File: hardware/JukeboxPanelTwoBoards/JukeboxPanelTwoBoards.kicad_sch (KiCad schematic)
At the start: 21 parts, among them J1 Raspberry_Pi_2_3, J2 Jukebox Panel, J3 +3.3V, J4 +5V, J5 GND, J6 Display Header, J7 8P8C

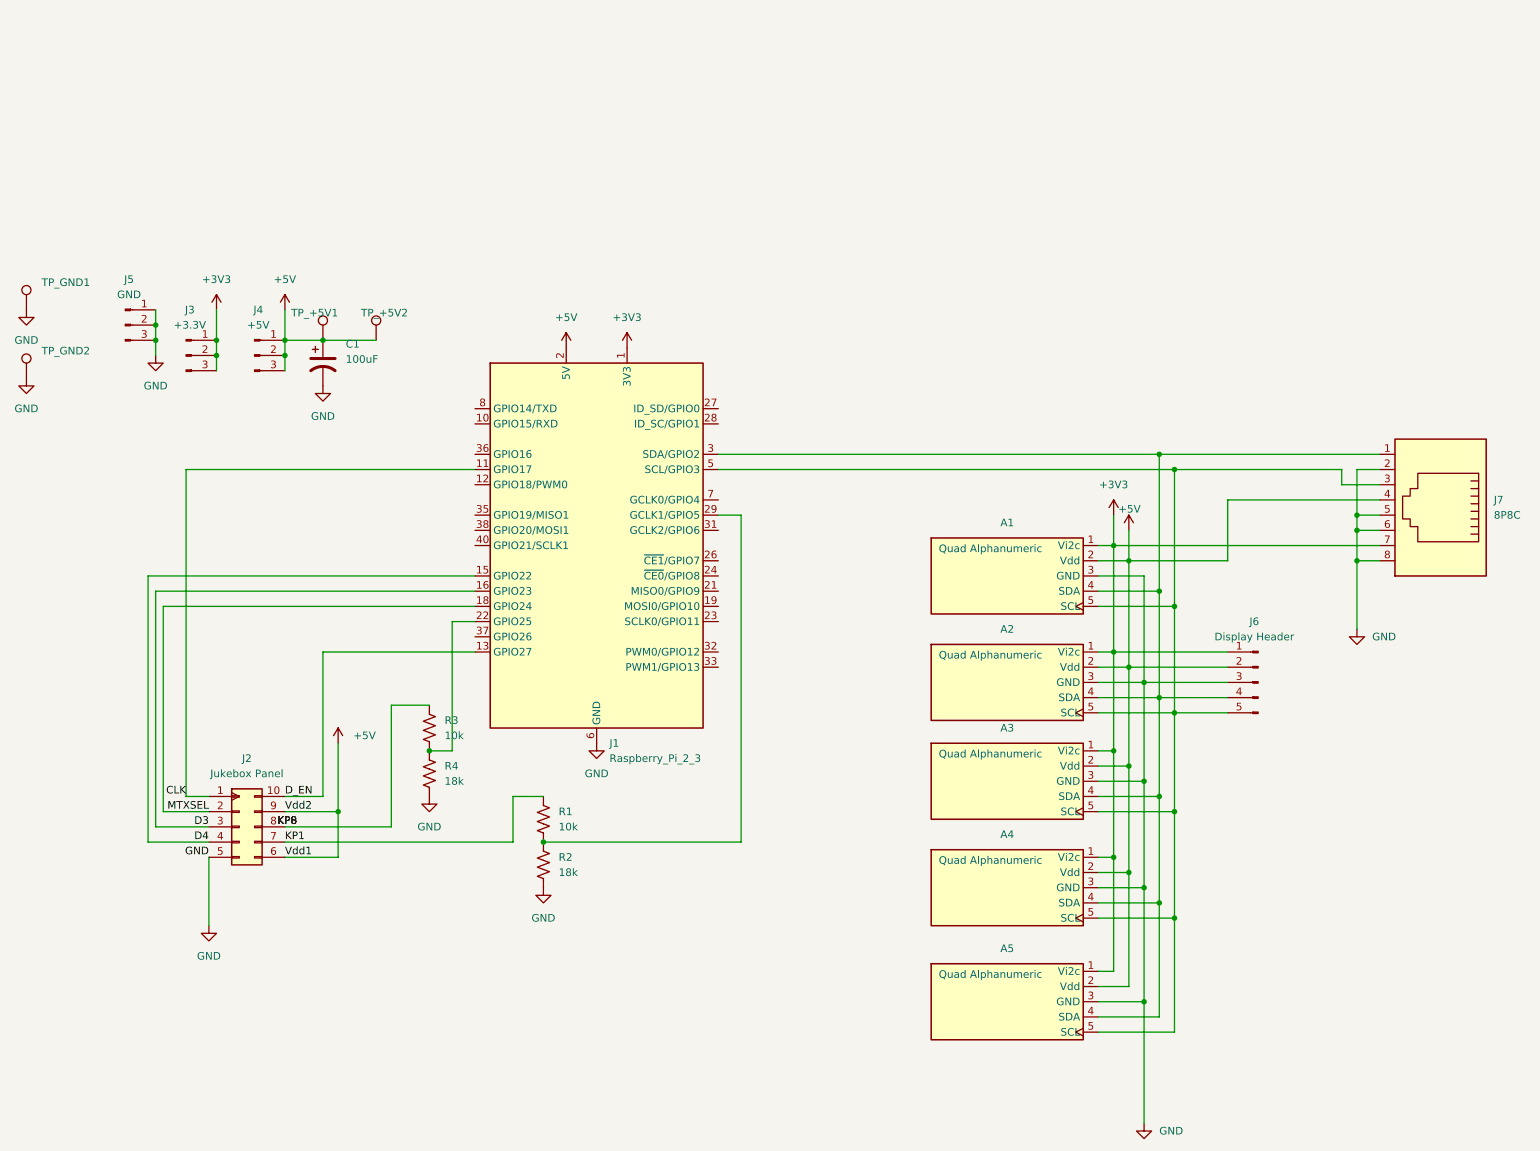
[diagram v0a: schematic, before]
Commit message: Add RJ45 8P8C connector schematic for JukeboxPanelTwoBoards
This commit introduces a new schematic file for the RJ45 8P8C connector used in the JukeboxPanelTwoBoards project. The schematic includes detailed properties, pin configurations, and global labels for power and signal connections. This addition enhances the project's documentation and supports future development and assembly processes.
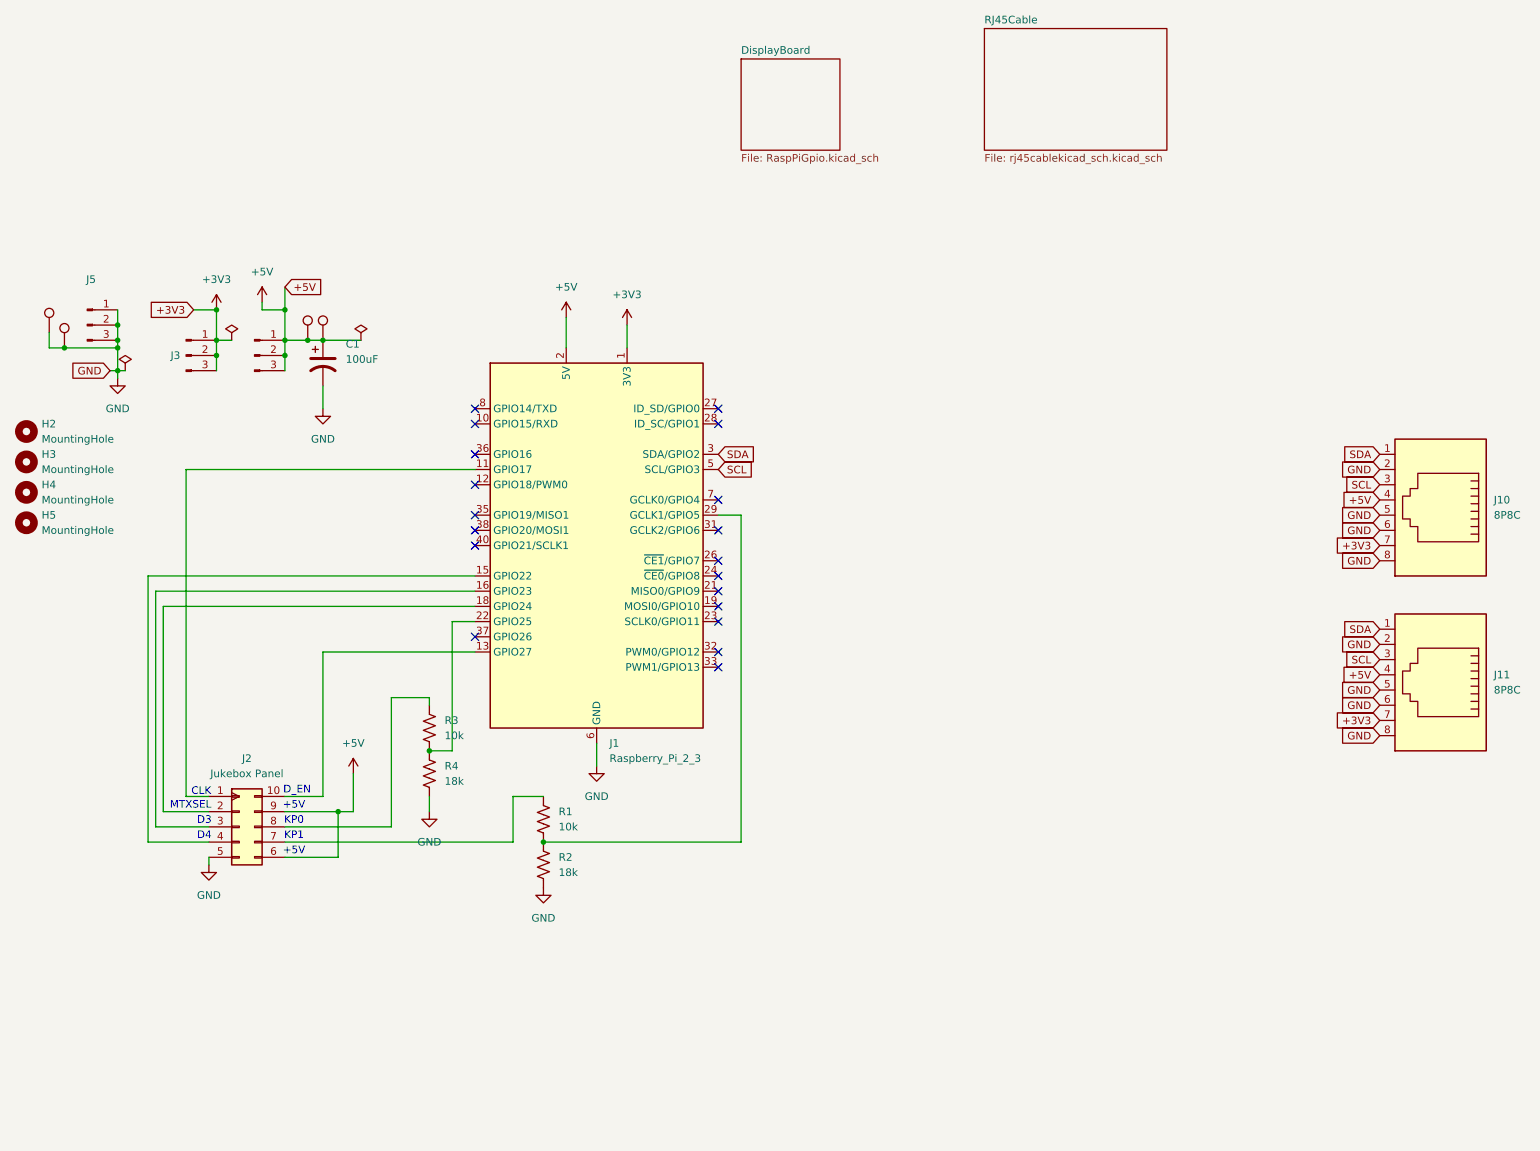
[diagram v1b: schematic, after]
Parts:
- removed A1, A2, A3, A4, A5: Quad Alphanumeric, MyParts:Adafruit_1911_QuadAlphaNum, symbol MyParts:Adafruit_1911_QuadAlphaNum
- removed J6: Display Header, Connector_PinHeader_2.54mm:PinHeader_1x05_P2.54mm_Vertical, symbol Connector:Conn_01x05_Pin
- removed TP_GND1: TestPoint, TestPoint:TestPoint_THTPad_D2.5mm_Drill1.2mm, symbol Connector:TestPoint
- added H2, H3, H4, H5: MountingHole, MountingHole:MountingHole_3.2mm_M3, symbol Mechanical:MountingHole
- added J11: 8P8C, Connector_RJ:RJ45_Ninigi_GE, symbol Connector:8P8C
- added TP_GND3: TestPoint, TestPoint:TestPoint_THTPad_D2.5mm_Drill1.2mm, symbol Connector:TestPoint
- renumbered J7 to J10
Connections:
- net +3V3: now also J11.7
- net +5V: now also J11.4
- net GND: now also J11.2, J11.5, J11.6, J11.8, TP_GND3.1
- net SDA: now reaches J1.3 (SDA/GPIO2), J10.1
- net SDA: now also J11.1
- net SCL: now reaches J1.5 (SCL/GPIO3), J10.3
- net SCL: now also J11.3
- net CLK: no longer names the net of J1.11 (GPIO17), J2.1 (CLK)
- net D3: no longer names the net of J1.16 (GPIO23), J2.3 (D3)
- net D4: no longer names the net of J1.15 (GPIO22), J2.4 (D4)
- net D_EN: no longer names the net of J1.13 (GPIO27), J2.10 (D_EN)
- net KP1: no longer names the net of J2.7 (KP1), R1.1
- net MTXSEL: no longer names the net of J1.18 (GPIO24), J2.2 (MTXSEL)
- no-connect marks 0 -> 19
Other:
- added sheet DisplayBoard (RaspPiGpio.kicad_sch)
- added sheet RJ45Cable (rj45cablekicad_sch.kicad_sch)
- note added: "+5V"
- note added: "CLK"
- note added: "D3"
- note added: "D4"
- note added: "D_EN"
- note added: "KP0"
- note added: "KP1"
- note added: "MTXSEL"
- moved on the sheet: J5
